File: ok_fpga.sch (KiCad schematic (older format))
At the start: 30 parts

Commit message: updates to FPGA page
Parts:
- removed J?: Conn_02x05_Odd_Even, symbol Connector_Generic:Conn_02x05_Odd_Even
- removed J?: Conn_02x10_Odd_Even, symbol Connector_Generic:Conn_02x10_Odd_Even
- removed R153, R154: 4.7k, Resistor_SMD:R_0603_1608Metric, symbol Device:R_US
- added R? (x2): DNI, Resistor_SMD:R_0603_1608Metric, symbol Device:R_US
- added U? (x2): TXS0108EPW, Package_SO:TSSOP-20_4.4x6.5mm_P0.65mm, symbol Logic_LevelTranslator:TXS0108EPW
- added U? (x2): TCA9555DBR, Package_SO:SSOP-24_5.3x8.2mm_P0.65mm, symbol Interface_Expansion:TCA9555DBR
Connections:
- net labels added: +5VA, 1V8_SCL, 1V8_SDA, DNO[1], DNO[2], DNO[3], DNO[4], DNO[5], DNO[6], DNO[7], DNO[8], DN[1], DN[2], DN[3], DN[4], DN[5], DN[6], DN[7], DN[8], DS1_CSB, DS1_SCLK, DS1_SDI, DS1_SDO, DS2_CSB, DS2_SCLK, DS2_SDI, DS2_SDO, EN_15V, EN_1V8, EN_3V3, EN_5V, EN_n15V, GPIO[0], GPIO[1], GPIO[2], GPIO[3], GPIO[4], GP_IO[0], GP_IO[1], GP_IO[2], GP_IO[3], GP_IO[4], GP_IO[5], GP_IO[6], GP_IO[7], G_DAC1[0..3], G_DAC1[0], G_DAC1[1], G_DAC1[2], G_DAC1[3], G_DAC2[0..3], G_DAC2[0], G_DAC2[1], G_DAC2[2], G_DAC2[3], G_DAC3[0..3], G_DAC3[0], G_DAC3[1], G_DAC3[2], G_DAC3[3], G_DAC4[0..3], G_DAC4[0], G_DAC4[1], G_DAC4[2], G_DAC4[3], G_DAC5[0..3], G_DAC5[0], G_DAC5[1], G_DAC5[2], G_DAC5[3], G_DAC6[0..3], G_DAC6[0], G_DAC6[1], G_DAC6[2], G_DAC6[3], LS_SCL, LS_SDA, UPO[1], UPO[2], UPO[3], UPO[4], UPO[5], UPO[6], UPO[7], UPO[8], UP[1], UP[2], UP[3], UP[4], UP[5], UP[6], UP[7], UP[8]
- net labels removed: DS_CSB, DS_SCLK, DS_SDI, DS_SDO, GP_0, GP_1, GP_10, GP_11, GP_2, GP_3, GP_4, GP_5, GP_6, GP_7, GP_8, GP_9, GP_SCL, GP_SDA, JP1-4, JP1-6, LS0_EN
- wire segments 239 -> 308
- no-connect marks 0 -> 12
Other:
- note added: "B>A"
- note added: "DOWN"
- note added: "SYS_CLK not special \nother than name"
- note added: "These are global (for all ADC channels)\nEN0 is the only signal that needs \nFPGA control per ADC channel.\nDefault settings: \nEN3,EN2,EN1,EN0 \n0,0,0,FPGA (A_EN2_HV is high-Z)\n\ndriving EN2 high outputs test\npatterns on the LVDS interface"
- note added: "UP"
- note removed: "11 @ 3.3V"
- note removed: "3 @ 3.3 V"
- note removed: "7 @ 3.3V"
- note removed: "SYS_CLK not special other than name"
- note removed: "These are global (for all ADC channels)\nEN0 is the only signal that needs FPGA control per ADC channel.\nDefault settings: \nEN3,EN2,EN1,EN0 \n0,0,0,FPGA (A_EN2_HV is high-Z)\n\ndriving EN2 high outputs test\npatterns on the LVDS interface"
- note removed: "board edge, 1.8 V signals"
- moved on the sheet: J?, R?, U?

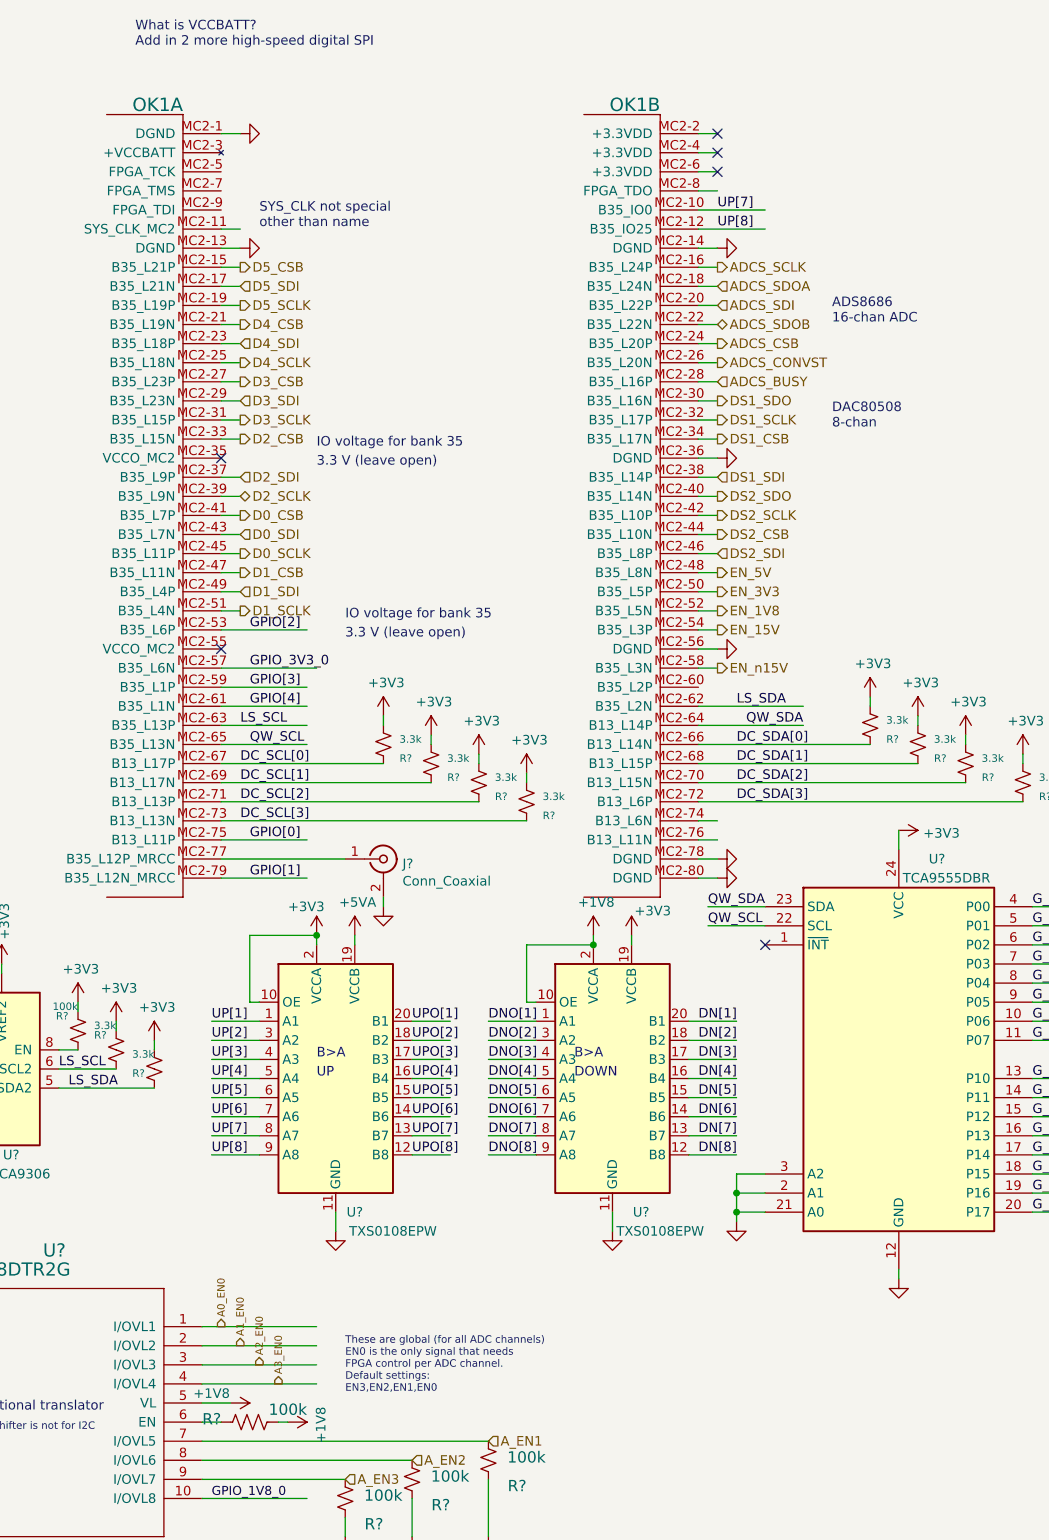
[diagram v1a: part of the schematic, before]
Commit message: modifications to power page for EN jumpers. Switched to all TI linear reg.
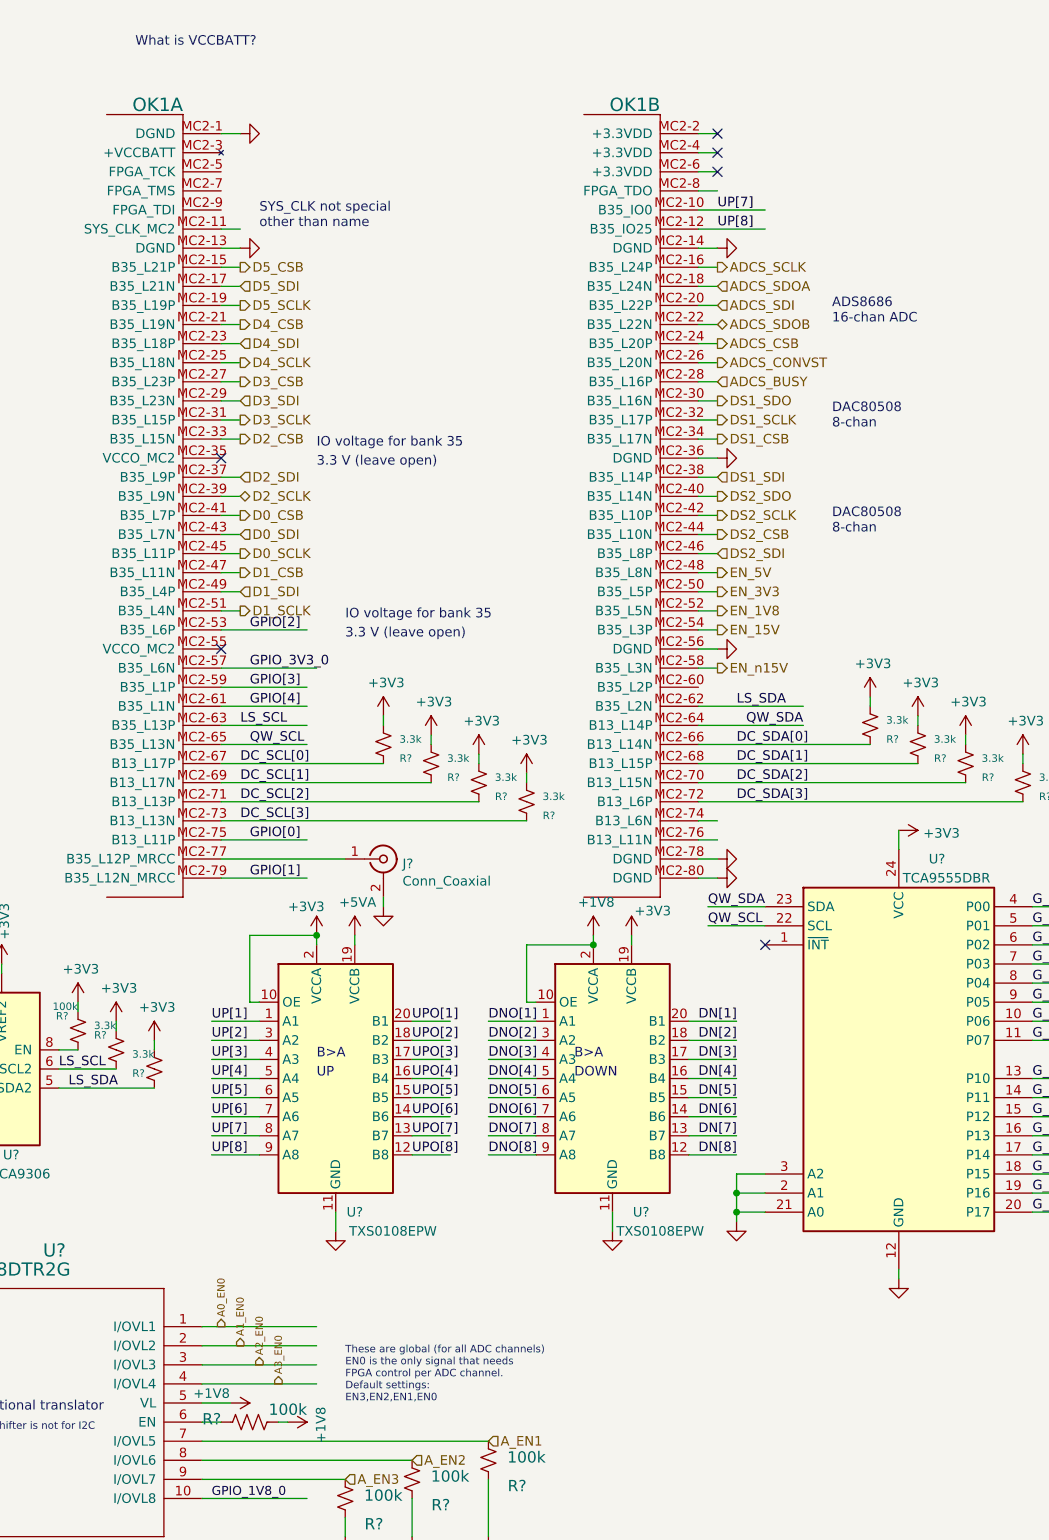
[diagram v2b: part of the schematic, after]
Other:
- note added: "What is VCCBATT?"
- note removed: "What is VCCBATT?\nAdd in 2 more high-speed digital SPI"
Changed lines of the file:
@@
 	1    0    0    -1
 $EndComp
-Text Notes 3550 7300 0    39   ~ 0
+Text Notes 3550 7350 0    39   ~ 0
 These are global (for all ADC channels)\nEN0 is the only signal that needs \nFPGA control per ADC channel.\nDefault settings: \nEN3,EN2,EN1,EN0 \n0,0,0,FPGA (A_EN2_HV is high-Z)\n\ndriving EN2 high outputs test\npatterns on the LVDS interface
 Entry Bus Bus
@@
 Text Label 3050 3500 0    50   ~ 0
 GPIO_3V3_0
-Text Notes 2450 250  0    50   ~ 0
-What is VCCBATT?\nAdd in 2 more high-speed digital SPI
 $Comp
 L power:+3V3 #PWR?
@@
 NoConn ~ 5500 800
 NoConn ~ 5500 700
+Text Notes 6100 2800 0    50   ~ 0
+DAC80508\n8-chan
 Wire Bus Line
 	11550 2600 11550 2900
@@
 Wire Bus Line
 	10350 5700 10350 6400
+Text Notes 2450 250  0    50   ~ 0
+What is VCCBATT?
 $EndSCHEMATC

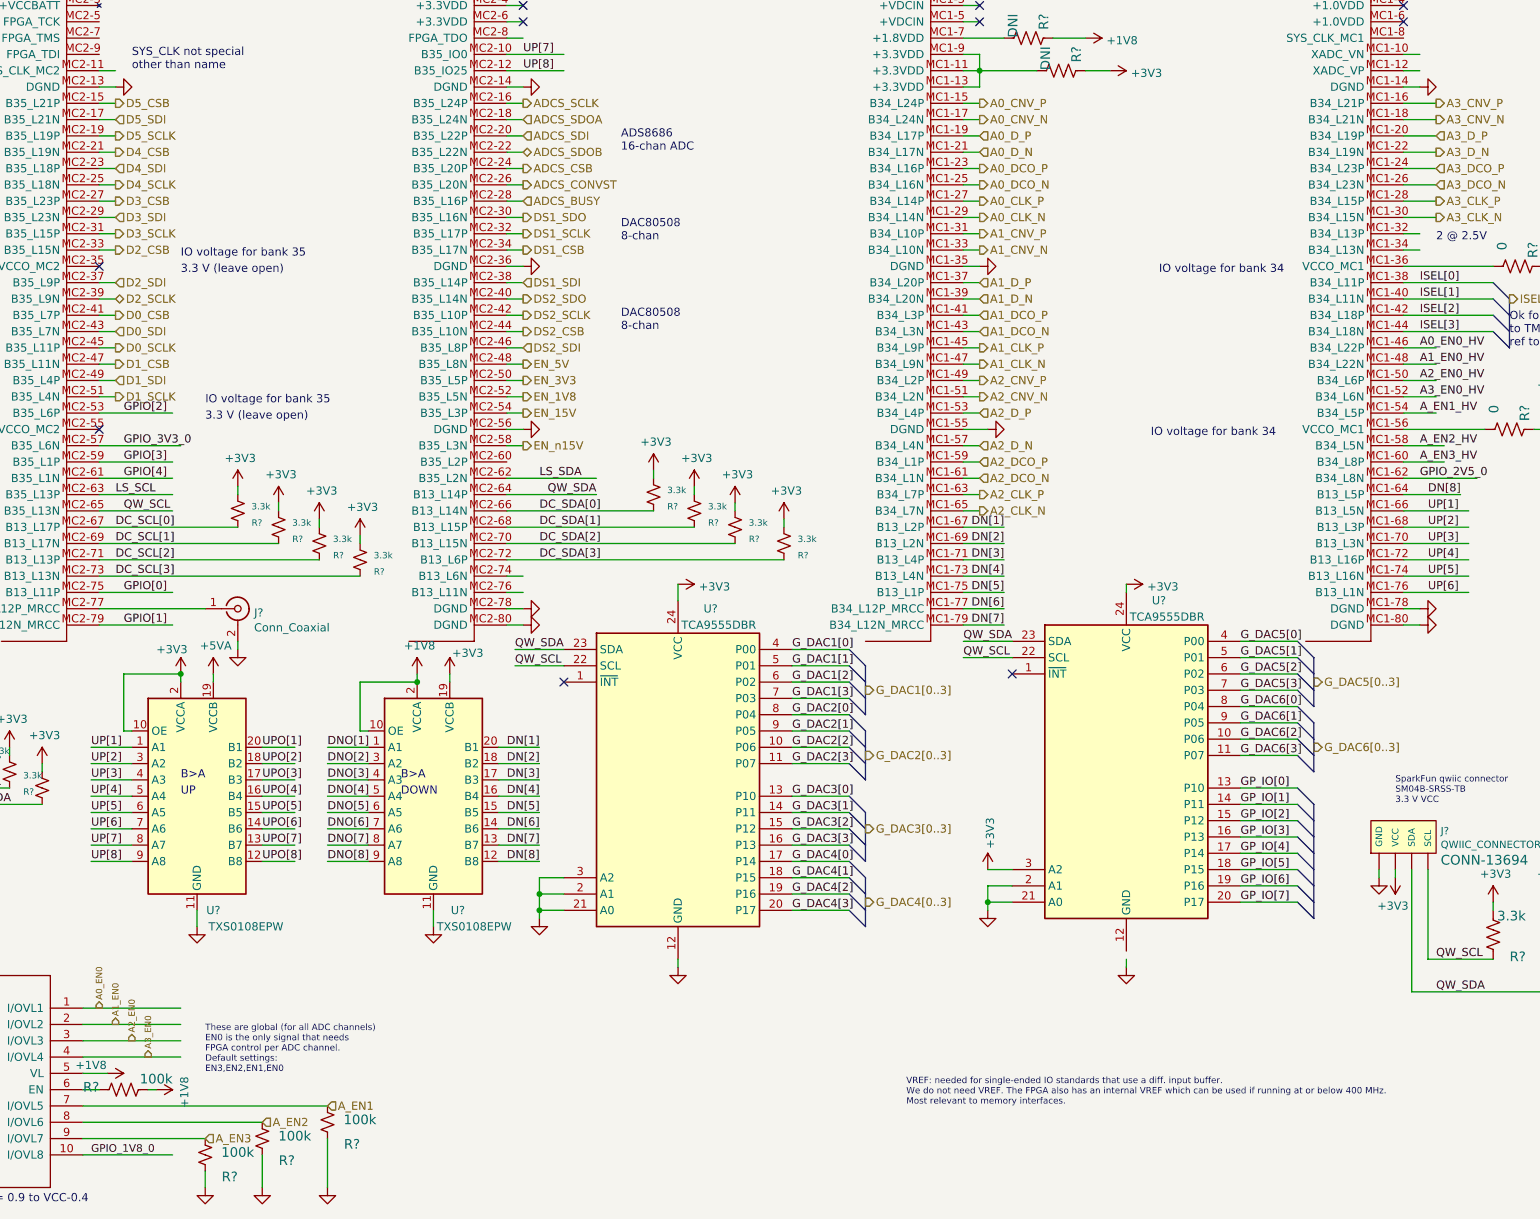
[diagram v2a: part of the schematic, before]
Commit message: top level almost connected
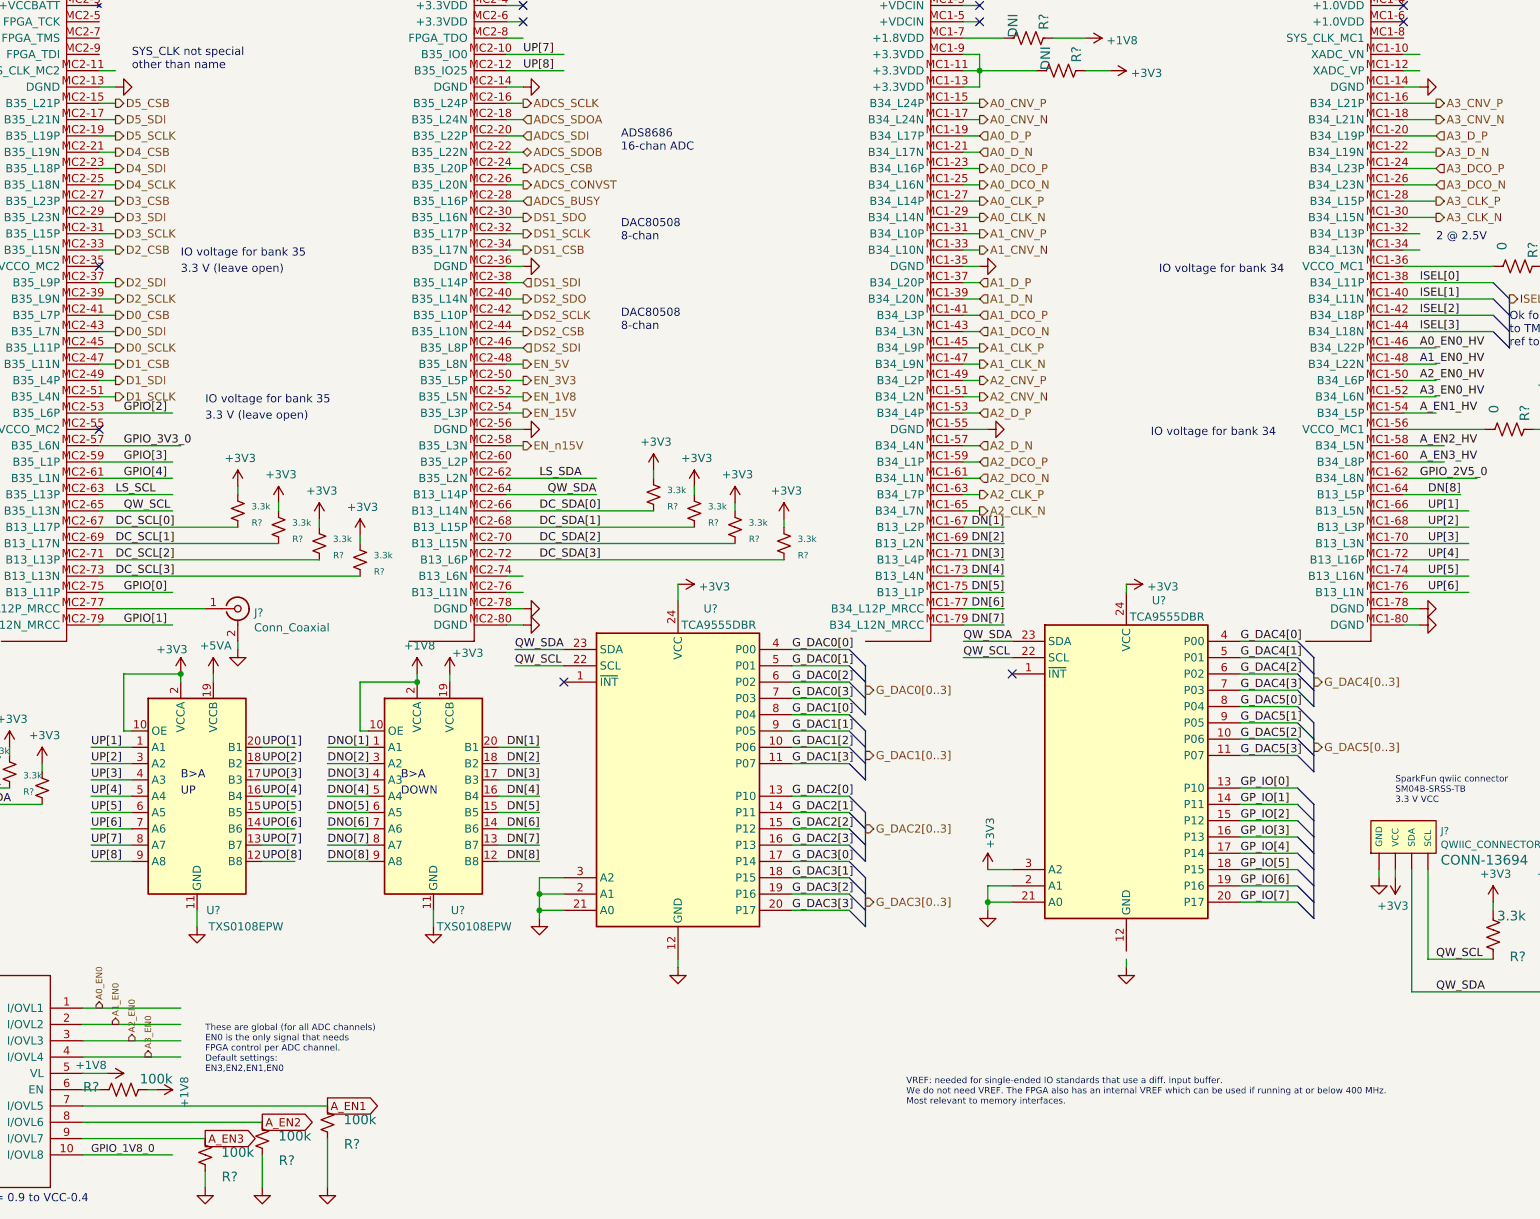
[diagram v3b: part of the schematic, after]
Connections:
- net labels added: G_DAC0[0..3], G_DAC0[0], G_DAC0[1], G_DAC0[2], G_DAC0[3]
- net labels removed: G_DAC6[0..3], G_DAC6[0], G_DAC6[1], G_DAC6[2], G_DAC6[3]
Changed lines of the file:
@@
 $Descr User 12505 8743
 encoding utf-8
-Sheet 6 10
+Sheet 5 18
 Title ""
 Date ""
@@
 Text HLabel 3000 2700 2    50   Output ~ 0
 D0_CSB
-Text HLabel 3000 2800 2    50   Input ~ 0
+Text HLabel 3000 2800 2    50   Output ~ 0
 D0_SDI
 Text HLabel 3000 2900 2    50   Output ~ 0
@@
 Text HLabel 3000 2000 2    50   Output ~ 0
 D3_CSB
-Text HLabel 3000 3100 2    50   Input ~ 0
+Text HLabel 3000 3100 2    50   Output ~ 0
 D1_SDI
 Text HLabel 3000 3200 2    50   Output ~ 0
@@
 Text HLabel 3000 3000 2    50   Output ~ 0
 D1_CSB
-Text HLabel 3000 2500 2    50   Input ~ 0
+Text HLabel 3000 2500 2    50   Output ~ 0
 D2_SDI
-Text HLabel 3000 2600 2    50   BiDi ~ 0
+Text HLabel 3000 2600 2    50   Output ~ 0
 D2_SCLK
 Text Label 11000 2900 0    50   ~ 0
@@
 Text HLabel 3000 2200 2    50   Output ~ 0
 D3_SCLK
-Text HLabel 3000 2100 2    50   Input ~ 0
+Text HLabel 3000 2100 2    50   Output ~ 0
 D3_SDI
 $Comp
@@
 Text Label 600  7150 0    39   ~ 0
 A2_EN0_HV
-Text HLabel 4300 7550 2    50   Input ~ 0
-A_EN1
 Wire Wire Line
 	3550 7950 3550 8050
@@
 Wire Wire Line
 	5400 4200 7100 4200
-Text HLabel 3550 7750 2    50   Input ~ 0
-A_EN3
 Wire Wire Line
 	2800 7450 2900 7450
@@
 	-1   0    0    -1
 $EndComp
-Text HLabel 3900 7650 2    50   Input ~ 0
-A_EN2
 $Comp
 L Interface:PCA9306 U?
@@
 Wire Wire Line
 	5500 2300 5400 2300
-Text HLabel 5500 2500 2    50   Input ~ 0
-DS1_SDI
 Text Notes 6100 1700 0    50   ~ 0
 ADS8686\n16-chan ADC
@@
 Text HLabel 3000 1900 2    50   Output ~ 0
 D4_SCLK
-Text HLabel 3000 1800 2    50   Input ~ 0
+Text HLabel 3000 1800 2    50   Output ~ 0
 D4_SDI
 Text HLabel 3000 1400 2    50   Output ~ 0
@@
 Text HLabel 3000 1600 2    50   Output ~ 0
 D5_SCLK
-Text HLabel 3000 1500 2    50   Input ~ 0
+Text HLabel 3000 1500 2    50   Output ~ 0
 D5_SDI
 $Comp
@@
 	7500 5050 7600 5150
 Text Label 7150 4750 0    50   ~ 0
+G_DAC0[0]
+Text Label 7150 4850 0    50   ~ 0
+G_DAC0[1]
+Text Label 7150 4950 0    50   ~ 0
+G_DAC0[2]
+Text Label 7150 5050 0    50   ~ 0
+G_DAC0[3]
+Text Label 7150 5150 0    50   ~ 0
 G_DAC1[0]
-Text Label 7150 4850 0    50   ~ 0
+Text Label 7150 5250 0    50   ~ 0
 G_DAC1[1]
-Text Label 7150 4950 0    50   ~ 0
+Text Label 7150 5350 0    50   ~ 0
 G_DAC1[2]
-Text Label 7150 5050 0    50   ~ 0
+Text Label 7150 5450 0    50   ~ 0
 G_DAC1[3]
-Text Label 7150 5150 0    50   ~ 0
+Text Label 7150 6350 0    50   ~ 0
+G_DAC3[3]
+Text Label 7150 6250 0    50   ~ 0
+G_DAC3[2]
+Text Label 7150 6150 0    50   ~ 0
+G_DAC3[1]
+Text Label 7150 6050 0    50   ~ 0
+G_DAC3[0]
+Text Label 7150 5950 0    50   ~ 0
+G_DAC2[3]
+Text Label 7150 5850 0    50   ~ 0
+G_DAC2[2]
+Text Label 7150 5750 0    50   ~ 0
+G_DAC2[1]
+Text Label 7150 5650 0    50   ~ 0
 G_DAC2[0]
-Text Label 7150 5250 0    50   ~ 0
-G_DAC2[1]
-Text Label 7150 5350 0    50   ~ 0
-G_DAC2[2]
-Text Label 7150 5450 0    50   ~ 0
-G_DAC2[3]
-Text Label 7150 6350 0    50   ~ 0
-G_DAC4[3]
-Text Label 7150 6250 0    50   ~ 0
-G_DAC4[2]
-Text Label 7150 6150 0    50   ~ 0
-G_DAC4[1]
-Text Label 7150 6050 0    50   ~ 0
-G_DAC4[0]
-Text Label 7150 5950 0    50   ~ 0
-G_DAC3[3]
-Text Label 7150 5850 0    50   ~ 0
-G_DAC3[2]
-Text Label 7150 5750 0    50   ~ 0
-G_DAC3[1]
-Text Label 7150 5650 0    50   ~ 0
-G_DAC3[0]
 $Comp
 L Interface_Expansion:TCA9555DBR U?
@@
 	9900 5000 10250 5000
 Text Label 9900 4700 0    50   ~ 0
+G_DAC4[0]
+Text Label 9900 4800 0    50   ~ 0
+G_DAC4[1]
+Text Label 9900 4900 0    50   ~ 0
+G_DAC4[2]
+Text Label 9900 5000 0    50   ~ 0
+G_DAC4[3]
+Text Label 9900 5100 0    50   ~ 0
 G_DAC5[0]
-Text Label 9900 4800 0    50   ~ 0
+Text Label 9900 5200 0    50   ~ 0
 G_DAC5[1]
-Text Label 9900 4900 0    50   ~ 0
+Text Label 9900 5300 0    50   ~ 0
 G_DAC5[2]
-Text Label 9900 5000 0    50   ~ 0
+Text Label 9900 5400 0    50   ~ 0
 G_DAC5[3]
-Text Label 9900 5100 0    50   ~ 0
-G_DAC6[0]
-Text Label 9900 5200 0    50   ~ 0
-G_DAC6[1]
-Text Label 9900 5300 0    50   ~ 0
-G_DAC6[2]
-Text Label 9900 5400 0    50   ~ 0
-G_DAC6[3]
 Text Label 9900 5600 0    50   ~ 0
 GP_IO[0]
@@
 LS_SCL
 Text HLabel 7600 5000 2    50   Output ~ 0
+G_DAC0[0..3]
+Text HLabel 7600 5400 2    50   Output ~ 0
 G_DAC1[0..3]
-Text HLabel 7600 5400 2    50   Output ~ 0
+Text HLabel 7600 5850 2    50   Output ~ 0
 G_DAC2[0..3]
-Text HLabel 7600 5850 2    50   Output ~ 0
+Text HLabel 7600 6300 2    50   Output ~ 0
 G_DAC3[0..3]
-Text HLabel 7600 6300 2    50   Output ~ 0
+Text HLabel 10350 5350 2    50   Output ~ 0
+G_DAC5[0..3]
+Text HLabel 10350 4950 2    50   Output ~ 0
 G_DAC4[0..3]
-Text HLabel 10350 5350 2    50   Output ~ 0
-G_DAC6[0..3]
-Text HLabel 10350 4950 2    50   Output ~ 0
-G_DAC5[0..3]
 Text HLabel 5500 2600 2    50   Output ~ 0
 DS2_SDO
@@
 Text Notes 6100 2800 0    50   ~ 0
 DAC80508\n8-chan
+Text Notes 2450 250  0    50   ~ 0
+What is VCCBATT?
 Wire Bus Line
 	11550 2600 11550 2900
@@
 Wire Bus Line
 	10350 5700 10350 6400
-Text Notes 2450 250  0    50   ~ 0
-What is VCCBATT?
+Text HLabel 5500 2500 2    50   Input ~ 0
+DS1_SDI
+Text GLabel 4300 7550 2    50   Output ~ 0
+A_EN1
+Text GLabel 3900 7650 2    50   Output ~ 0
+A_EN2
+Text GLabel 3550 7750 2    50   Output ~ 0
+A_EN3
 $EndSCHEMATC
